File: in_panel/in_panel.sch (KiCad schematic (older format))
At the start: 0 parts

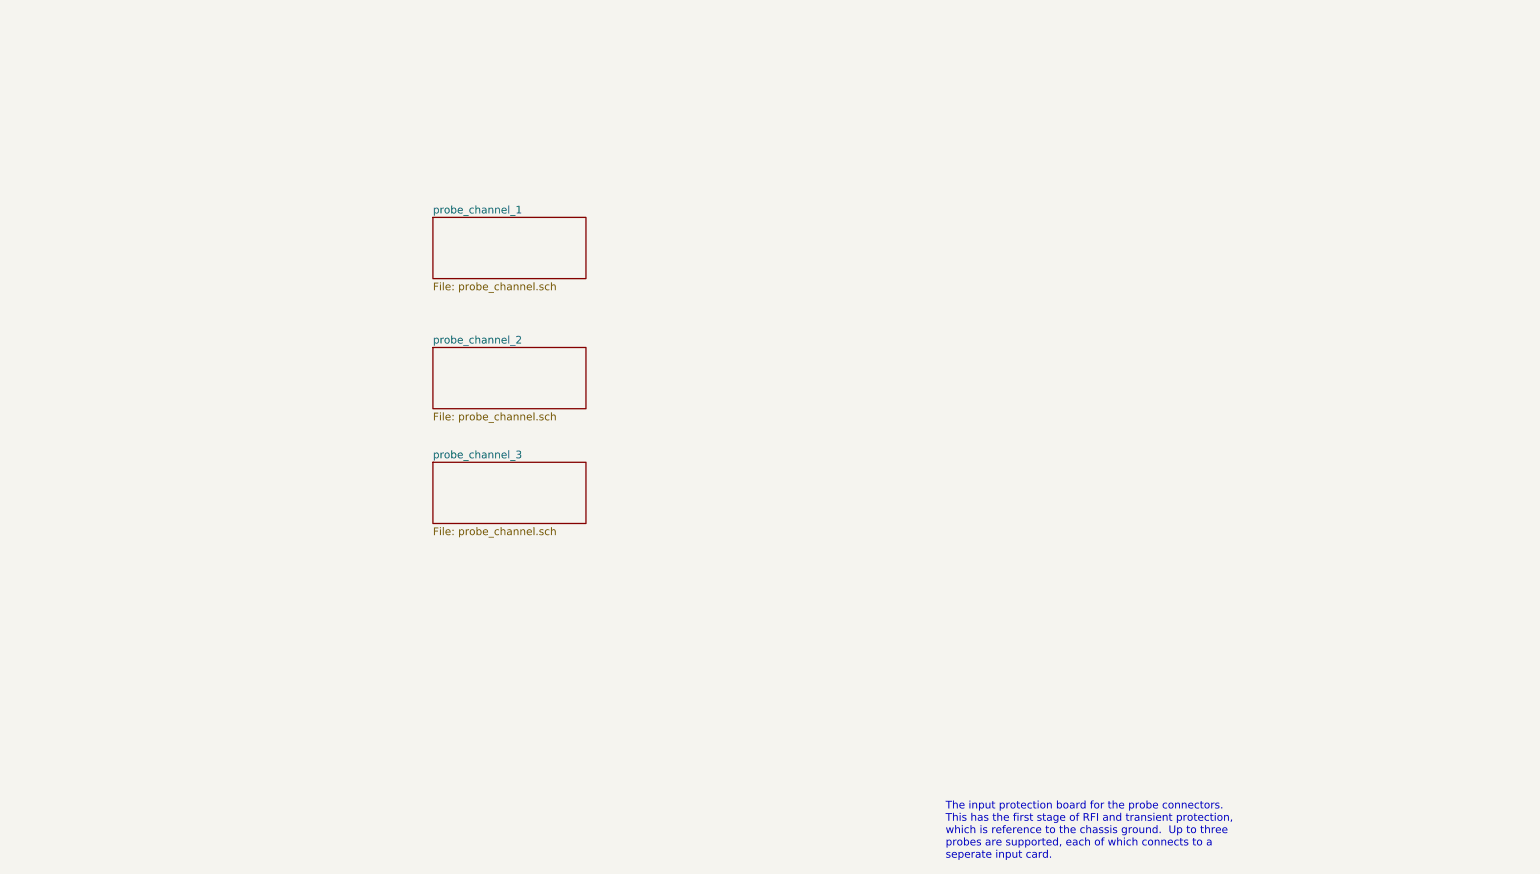
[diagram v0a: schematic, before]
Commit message: in_panel is nearly complete, input/adc.sch: change testpoint style to loop. input/input_channel.sch: modification seems spurious
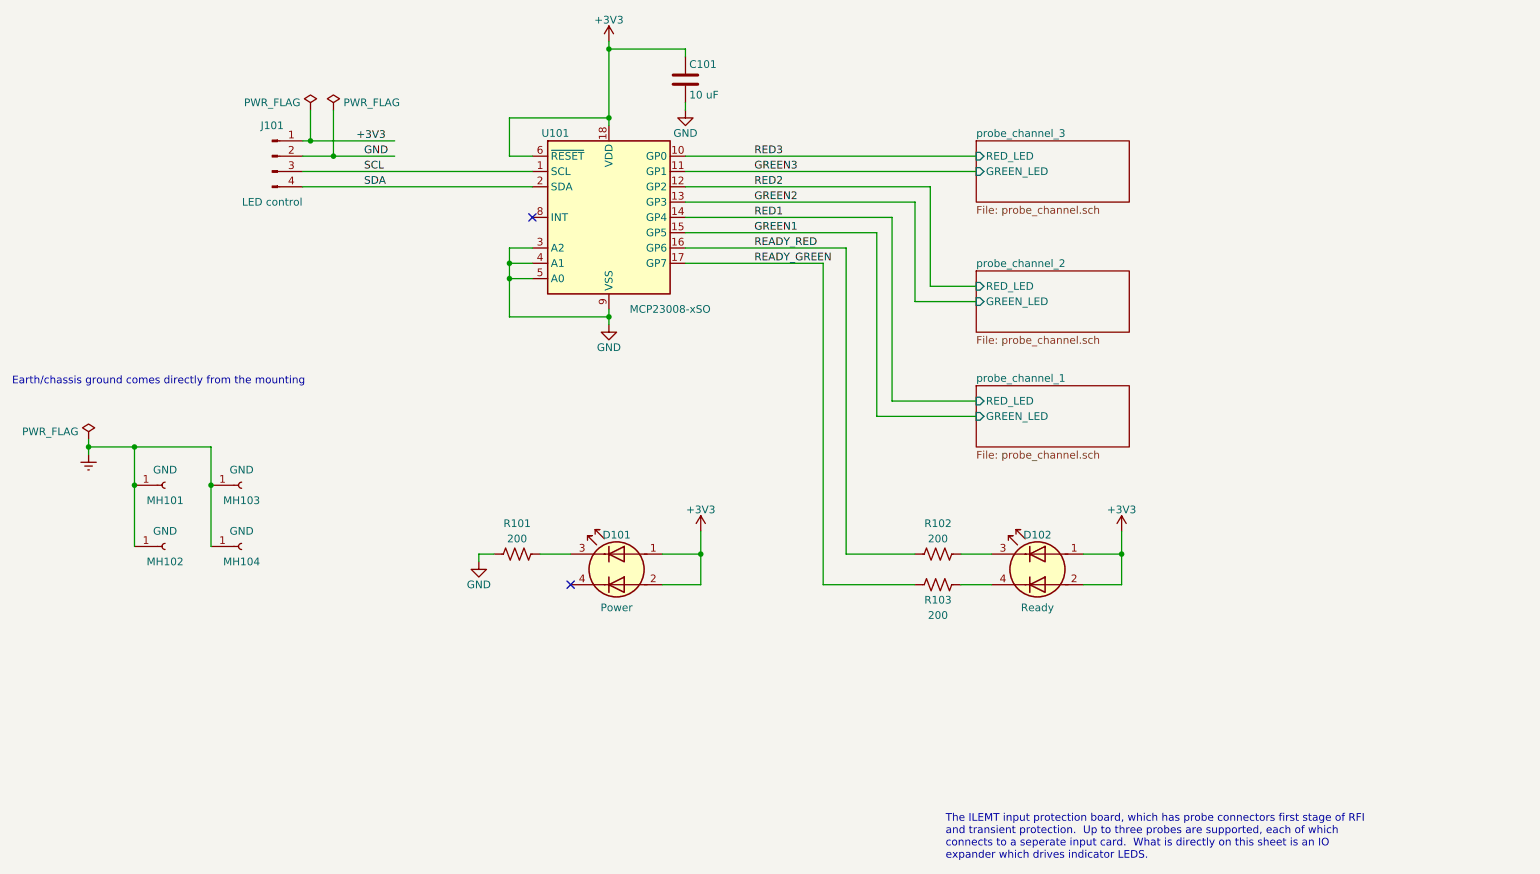
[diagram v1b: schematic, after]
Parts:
- added C101: 10 uF, Capacitor_SMD:C_0603_1608Metric, symbol Device:C
- added D101: Power, input:LED_Wurth-PLCC4_3.2x2.8mm, symbol Device:LED_Dual_AACC
- added D102: Ready, input:LED_Wurth-PLCC4_3.2x2.8mm, symbol Device:LED_Dual_AACC
- added J101: LED control, input:molex_kk100_PinHeader_1x4_P2.54_Drill1.1mm, symbol Connector:Conn_01x04_Male
- added MH101, MH102, MH103, MH104: GND, MountingHole:MountingHole_3.2mm_M3_Pad, symbol Connector:Conn_01x01_Female
- added R101, R102, R103: 200, Resistor_SMD:R_0603_1608Metric, symbol Device:R_US
- added U101: MCP23008-xSO, Package_SO:SOIC-18W_7.5x11.6mm_P1.27mm, symbol Interface_Expansion:MCP23008-xSO
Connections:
- net labels added: +3V3, Earth, GND, GREEN1, GREEN2, GREEN3, READY_GREEN, READY_RED, RED1, RED2, RED3, SCL, SDA
- wire segments 0 -> 67
- no-connect marks 0 -> 2
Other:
- note added: "Earth/chassis ground comes directly from the mounting"
- note added: "The ILEMT input protection board, which has probe connectors first stage of RFI\nand transient protection. Up to three probes are supported, each of which\nconnects to a seperate input card. What is directly on this sheet is an IO\nexpander which drives indicator LEDS.\n"
- note removed: "The input protection board for the probe connectors.\nThis has the first stage of RFI and transient protection,\nwhich is reference to the chassis ground. Up to three \nprobes are supported, each of which connects to a\nseperate input card."

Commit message: Revision 0 of in_panel, off to fab
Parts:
- D101, D102: DK line (none) -> IP.3; Description (none) -> LED GREEN/RED CLEAR 3528 SMD; Digikey (none) -> 732-5001-1-ND; MPN (none) -> 150141RV73100; Manufacturer (none) -> Würth Elektronik
- J101: DK line (none) -> IP.6; Description (none) -> CONN HEADER VERT 4POS 2.54MM; Digikey (none) -> WM4202-ND; MPN (none) -> 0022232041; Manufacturer (none) -> Molex
- MH101, MH102, MH103, MH104: Description (none) -> Mounting hole; MPN (none) -> DNP
- R101, R102, R103: DK line (none) -> I.55; Description (none) -> RES 200 OHM 1% 1/8W 0603; Digikey (none) -> RNCP0603FTD200RCT-ND; MPN (none) -> RNCP0603FTD200R; Manufacturer (none) -> Stackpole Electronics Inc
- U101: DK line (none) -> IP.4; Description (none) -> IC I/O EXPANDER I2C 8B 18SOIC; Digikey (none) -> MCP23008-E/SO-ND; MPN (none) -> MCP23008-E/SO; Manufacturer (none) -> Microchip Technology
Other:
- note added: "Earth/chassis ground comes directly from the mounting.\nThere is no connection on this board between chassis\nground and the GND used for the LED control."
- note added: "The ILEMT input protection board, which has the probe connectors and first stage\nof RFI and transient protection. Up to three probes are supported, each of\nwhich connects to a seperate input card. What is directly on this sheet is an\nIO expander which drives indicator LEDS.\n"
- note removed: "Earth/chassis ground comes directly from the mounting"
- note removed: "The ILEMT input protection board, which has probe connectors first stage of RFI\nand transient protection. Up to three probes are supported, each of which\nconnects to a seperate input card. What is directly on this sheet is an IO\nexpander which drives indicator LEDS.\n"
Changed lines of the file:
@@
 $EndSheet
 Text Notes 7150 7000 0    50   ~ 0
-The ILEMT input protection board, which has probe connectors first stage of RFI\nand transient protection.  Up to three probes are supported, each of which\nconnects to a seperate input card.  What is directly on this sheet is an IO\nexpander which drives indicator LEDS.\n
+The ILEMT input protection board, which has the probe connectors and first stage\nof RFI and transient protection.  Up to three probes are supported, each of\nwhich connects to a seperate input card.  What is directly on this sheet is an\nIO expander which drives indicator LEDS.\n
 $Comp
 L Interface_Expansion:MCP23008-xSO U?
@@
 F 2 "Package_SO:SOIC-18W_7.5x11.6mm_P1.27mm" H 4950 1750 50  0001 C CNN
 F 3 "http://ww1.microchip.com/downloads/en/DeviceDoc/MCP23008-MCP23S08-Data-Sheet-20001919F.pdf" H 6250 1600 50  0001 C CNN
+F 4 "IP.4" H 4950 2800 50  0001 C CNN "DK line"
+F 5 "IC I/O EXPANDER I2C 8B 18SOIC" H 4950 2800 50  0001 C CNN "Description"
+F 6 "MCP23008-E/SO-ND" H 4950 2800 50  0001 C CNN "Digikey"
+F 7 "MCP23008-E/SO" H 4950 2800 50  0001 C CNN "MPN"
+F 8 "Microchip Technology" H 4950 2800 50  0001 C CNN "Manufacturer"
 	1    4950 2800
 	1    0    0    -1
@@
 F 1 "LED control" H 2750 2100 50  0000 C CNN
 F 2 "input:molex_kk100_PinHeader_1x4_P2.54_Drill1.1mm" H 2750 2400 50  0001 C CNN
-F 3 "~" H 2750 2400 50  0001 C CNN
+F 3 "https://www.molex.com/pdm_docs/sd/022232041_sd.pdf" H 2750 2400 50  0001 C CNN
+F 4 "IP.6" H 2750 2400 50  0001 C CNN "DK line"
+F 5 "CONN HEADER VERT 4POS 2.54MM" H 2750 2400 50  0001 C CNN "Description"
+F 6 "WM4202-ND" H 2750 2400 50  0001 C CNN "Digikey"
+F 7 "0022232041" H 2750 2400 50  0001 C CNN "MPN"
+F 8 "Molex" H 2750 2400 50  0001 C CNN "Manufacturer"
 	1    2750 2400
 	1    0    0    -1
@@
 	1550 4250 1550 4300
 Text Notes 1050 3900 0    50   ~ 0
-Earth/chassis ground comes directly from the mounting
+Earth/chassis ground comes directly from the mounting.\nThere is no connection on this board between chassis\nground and the GND used for the LED control.
 Text Label 3350 2500 0    50   ~ 0
 SCL
@@
 F 1 "Ready" H 7750 4850 50  0000 C CNN
 F 2 "input:LED_Wurth-PLCC4_3.2x2.8mm" H 7780 5100 50  0001 C CNN
-F 3 "~" H 7780 5100 50  0001 C CNN
+F 3 "https://katalog.we-online.de/led/datasheet/150141RV73100.pdf" H 7780 5100 50  0001 C CNN
+F 4 "150141RV73100" H 7750 5100 50  0001 C CNN "MPN"
+F 5 "IP.3" H 7750 5100 50  0001 C CNN "DK line"
+F 6 "LED GREEN/RED CLEAR 3528 SMD" H 7750 5100 50  0001 C CNN "Description"
+F 7 "732-5001-1-ND" H 7750 5100 50  0001 C CNN "Digikey"
+F 8 "Würth Elektronik" H 7750 5100 50  0001 C CNN "Manufacturer"
 	1    7750 5100
 	-1   0    0    -1
@@
 F 2 "Resistor_SMD:R_0603_1608Metric" V 7140 4990 50  0001 C CNN
 F 3 "~" H 7100 5000 50  0001 C CNN
+F 4 "I.55" H 7100 5000 50  0001 C CNN "DK line"
+F 5 "RES 200 OHM 1% 1/8W 0603" H 7100 5000 50  0001 C CNN "Description"
+F 6 "RNCP0603FTD200RCT-ND" H 7100 5000 50  0001 C CNN "Digikey"
+F 7 "RNCP0603FTD200R" H 7100 5000 50  0001 C CNN "MPN"
+F 8 "Stackpole Electronics Inc" H 7100 5000 50  0001 C CNN "Manufacturer"
 	1    7100 5000
 	0    1    1    0
@@
 F 2 "Resistor_SMD:R_0603_1608Metric" V 7140 5190 50  0001 C CNN
 F 3 "~" H 7100 5200 50  0001 C CNN
+F 4 "I.55" H 7100 5200 50  0001 C CNN "DK line"
+F 5 "RES 200 OHM 1% 1/8W 0603" H 7100 5200 50  0001 C CNN "Description"
+F 6 "RNCP0603FTD200RCT-ND" H 7100 5200 50  0001 C CNN "Digikey"
+F 7 "RNCP0603FTD200R" H 7100 5200 50  0001 C CNN "MPN"
+F 8 "Stackpole Electronics Inc" H 7100 5200 50  0001 C CNN "Manufacturer"
 	1    7100 5200
 	0    1    1    0
@@
 F 1 "Power" H 5000 4850 50  0000 C CNN
 F 2 "input:LED_Wurth-PLCC4_3.2x2.8mm" H 5030 5100 50  0001 C CNN
-F 3 "~" H 5030 5100 50  0001 C CNN
+F 3 "https://katalog.we-online.de/led/datasheet/150141RV73100.pdf" H 5030 5100 50  0001 C CNN
+F 4 "150141RV73100" H 5000 5100 50  0001 C CNN "MPN"
+F 5 "IP.3" H 5000 5100 50  0001 C CNN "DK line"
+F 6 "LED GREEN/RED CLEAR 3528 SMD" H 5000 5100 50  0001 C CNN "Description"
+F 7 "732-5001-1-ND" H 5000 5100 50  0001 C CNN "Digikey"
+F 8 "Würth Elektronik" H 5000 5100 50  0001 C CNN "Manufacturer"
 	1    5000 5100
 	-1   0    0    -1
@@
 F 2 "Resistor_SMD:R_0603_1608Metric" V 4390 4990 50  0001 C CNN
 F 3 "~" H 4350 5000 50  0001 C CNN
+F 4 "I.55" H 4350 5000 50  0001 C CNN "DK line"
+F 5 "RES 200 OHM 1% 1/8W 0603" H 4350 5000 50  0001 C CNN "Description"
+F 6 "RNCP0603FTD200RCT-ND" H 4350 5000 50  0001 C CNN "Digikey"
+F 7 "RNCP0603FTD200R" H 4350 5000 50  0001 C CNN "MPN"
+F 8 "Stackpole Electronics Inc" H 4350 5000 50  0001 C CNN "Manufacturer"
 	1    4350 5000
 	0    1    1    0
@@
 F 2 "MountingHole:MountingHole_3.2mm_M3_Pad" H 2050 4550 50  0001 C CNN
 F 3 "~" H 2050 4550 50  0001 C CNN
+F 4 "Mounting hole" H 2050 4550 50  0001 C CNN "Description"
+F 5 "DNP" H 2050 4550 50  0001 C CNN "MPN"
 	1    2050 4550
 	1    0    0    1
@@
 F 2 "MountingHole:MountingHole_3.2mm_M3_Pad" H 2050 4950 50  0001 C CNN
 F 3 "~" H 2050 4950 50  0001 C CNN
+F 4 "Mounting hole" H 2050 4950 50  0001 C CNN "Description"
+F 5 "DNP" H 2050 4950 50  0001 C CNN "MPN"
 	1    2050 4950
 	1    0    0    1
@@
 F 2 "MountingHole:MountingHole_3.2mm_M3_Pad" H 2550 4950 50  0001 C CNN
 F 3 "~" H 2550 4950 50  0001 C CNN
+F 4 "Mounting hole" H 2550 4950 50  0001 C CNN "Description"
+F 5 "DNP" H 2550 4950 50  0001 C CNN "MPN"
 	1    2550 4950
 	1    0    0    1
@@
 F 2 "MountingHole:MountingHole_3.2mm_M3_Pad" H 2550 4550 50  0001 C CNN
 F 3 "~" H 2550 4550 50  0001 C CNN
+F 4 "Mounting hole" H 2550 4550 50  0001 C CNN "Description"
+F 5 "DNP" H 2550 4550 50  0001 C CNN "MPN"
 	1    2550 4550
 	1    0    0    1
